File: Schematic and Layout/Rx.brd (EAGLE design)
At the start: 44.5 x 80 mm, 21 parts

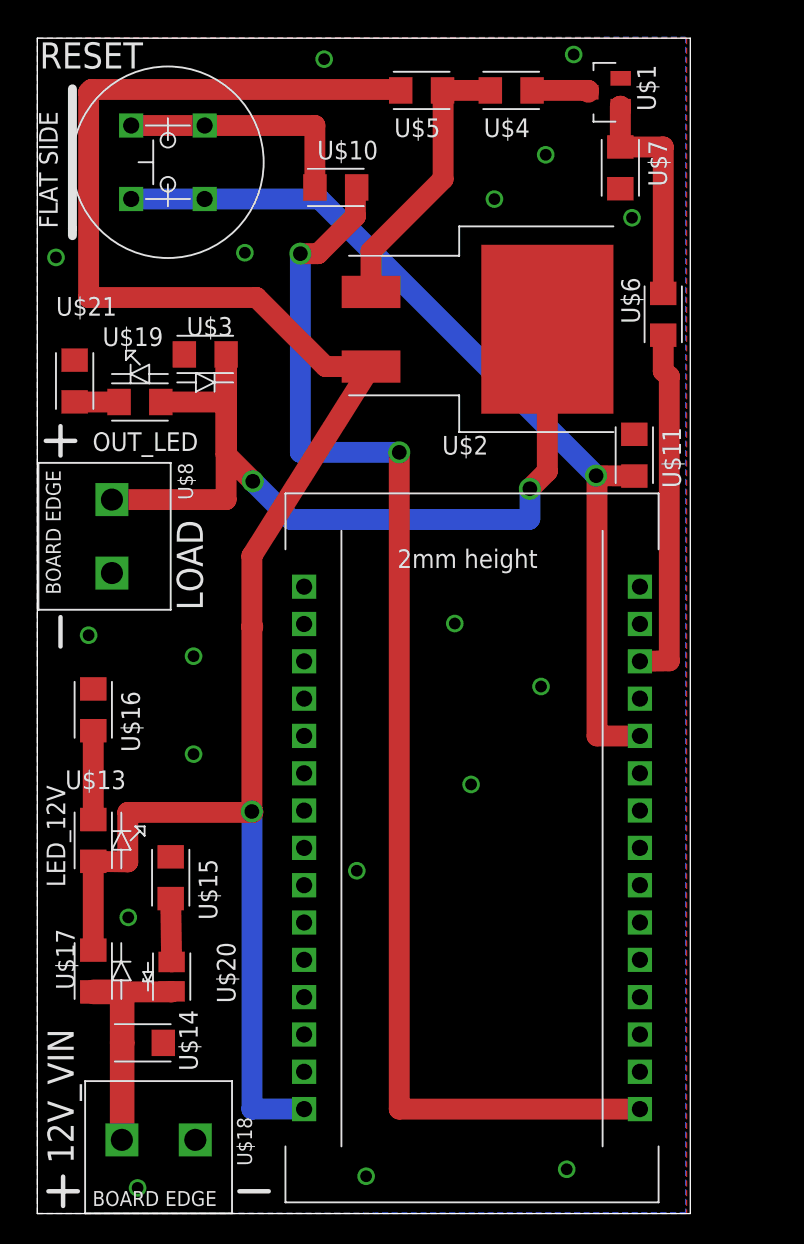
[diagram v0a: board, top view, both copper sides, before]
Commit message: ESPs now run off of 5 V
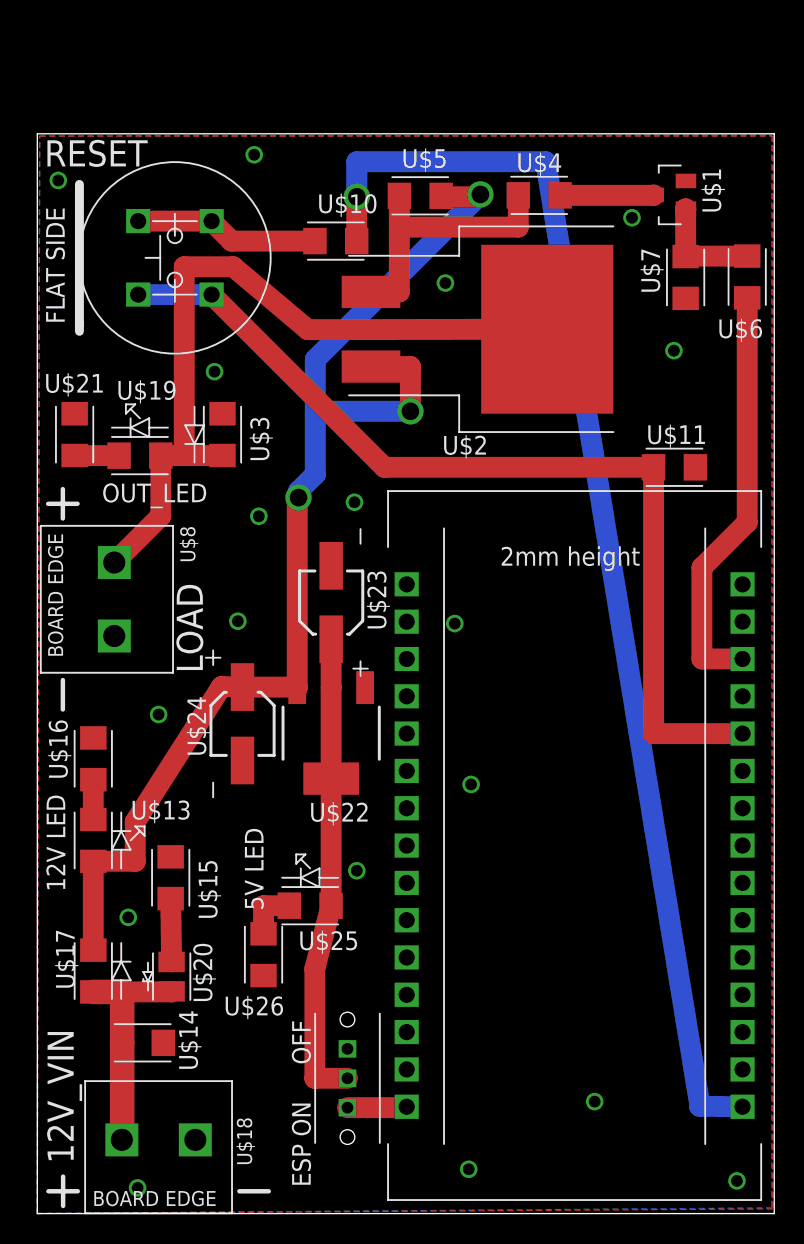
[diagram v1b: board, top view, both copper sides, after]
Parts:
- added U$22: 5V_REG, Gas_Sensor_Lib_v1:SOT223
- added U$23, U$24: 10uF, Gas_Sensor_Lib_v1:153CLV-0405
- added U$25: LED_5V, Gas_Sensor_Lib_v1:LED_1206
- added U$26: 1K, Gas_Sensor_Lib_v1:R1206
- added U$27: SPDT, Gas_Sensor_Lib_v1:SPDT
- moved U$7 8.68 mm to (44.1, 63.7)
- moved U$1 8.28 mm to (43.1, 69.3)
- moved U$4 7.39 mm to (34.2, 69.3)
- moved U$5 7.18 mm to (26.1, 69.3), turned to 0 degrees
- moved U$9 6.99 mm to (36.6, 25.1)
- moved U$12 6.53 mm to (9.37, 65.1)
- moved U$6 6.25 mm to (48.3, 63.8)
- moved U$3 5.59 mm to (12.6, 53.0), turned to 270 degrees
- moved U$8 4.29 mm to (5.24, 41.8)
- moved U$19 3.65 mm to (6.99, 51.6)
- moved U$21 3.65 mm to (2.54, 53.0)
- moved U$10 3.65 mm to (20.3, 66.2)
- moved U$16 3.33 mm to (3.81, 31.0)
- moved U$11 2.85 mm to (43.4, 50.8), turned to 180 degrees
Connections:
- new net 5V: U$22.2, U$22.4, U$23.+, U$25.1, U$27.IN
- new net N$13: U$27.A, U$9.VIN
- new net N$8: U$25.2, U$26.2
- net 12V: now also U$22.3, U$24.+; no longer U$9.VIN
- net GND: now also U$22.1, U$23.-, U$24.-, U$26.1
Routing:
- net 12V: track 133.4 -> 81.8 mm, vias 1 -> 3
- net 5V: track 0.00 -> 32.3 mm
- net N$6: track 65.0 -> 51.9 mm, vias 2 -> 0
- net N$1: track 15.7 -> 7.49 mm
- net N$2: track 24.4 -> 28.6 mm
- net N$9: track 16.7 -> 12.6 mm
- net N$13: track 0.00 -> 4.10 mm
- net N$8: track 0.00 -> 3.66 mm
- net N$11: track 6.05 -> 2.71 mm
- net N$3: track 3.95 -> 6.40 mm
- net N$10: track 88.1 -> 86.3 mm, vias 2 -> 1
- net N$7: track 62.7 -> 64.1 mm, vias 1 -> 0
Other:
- board size 44.5 x 80 mm -> 50.2 x 73.5 mm
- board text added: "12V LED"
- board text added: "5V LED"
- board text removed: "LED_12V"
